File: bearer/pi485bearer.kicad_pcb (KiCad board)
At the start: 2 copper layers, 62 x 30 mm, 24 parts, among them P1 PWR, P2 Rasperry Pi, P5 CONN_01X04, P6 CONN_01X04, Q1 2N4401, Q2 2N4401, Q3 2N4401, U1 NE555

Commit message: Some additional cleanup and re-routing
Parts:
- removed MNT01 (x2), MNT02: MountingHole_2.2mm_M2, Mounting_Holes:MountingHole_2.2mm_M2
- removed RO: RO, Pin_Headers:Pin_Header_Straight_1x02
- removed TERM: TERM, Pin_Headers:Pin_Header_Straight_1x02
- added P3: RO, Pin_Headers:Pin_Header_Straight_1x02, F.Cu at (83.2, 24.8)
- added P4: TERM, Pin_Headers:Pin_Header_Straight_1x02, F.Cu at (94.6, 29.8)
- R7: value R -> 120
- moved R7 2.54 mm to (90.8, 33.0)
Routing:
- net GND: track 125.0 -> 128.6 mm
- net /lctec485/B: track 12.0 -> 10.8 mm
- net /lctec485/A: track 3.81 -> 4.86 mm
- net /lctec485/VCIN: track 90.0 -> 89.4 mm
- net Net-(P4-Pad2): track 4.34 -> 3.70 mm

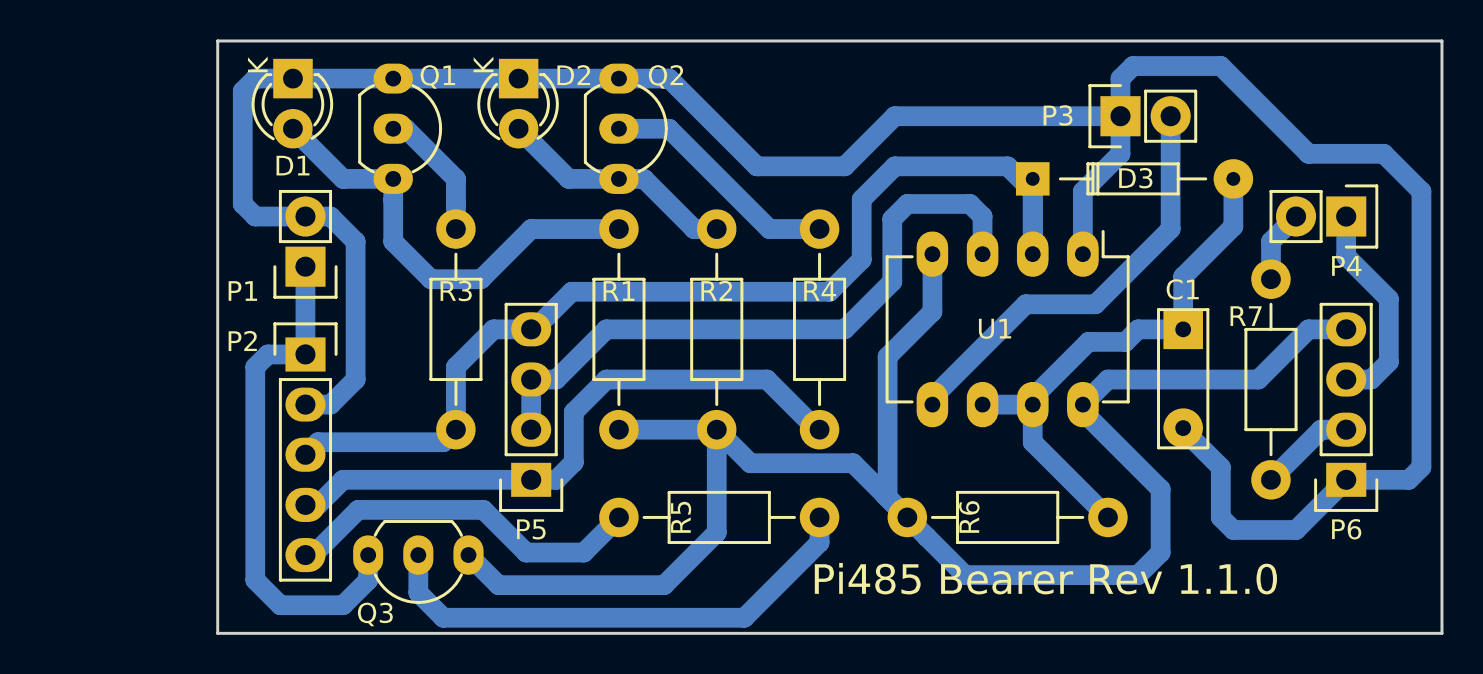
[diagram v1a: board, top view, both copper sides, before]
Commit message: Low-side NPN switching. We'll see if things 'floating' causes issues... if so, I'll have to order a few PNP's to use for high-side switching.
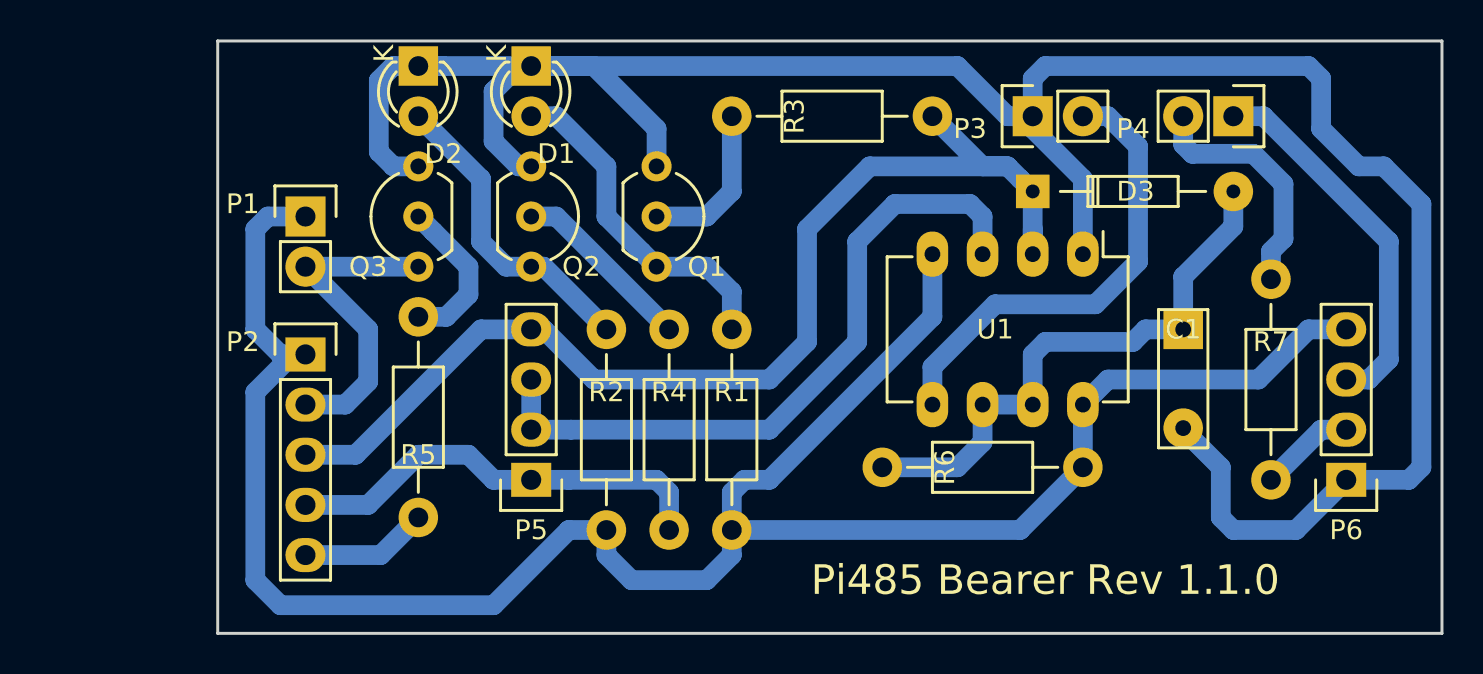
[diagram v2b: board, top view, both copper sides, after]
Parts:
- moved R5 22.7 mm to (47.6, 34.9), turned to 270 degrees
- moved R3 15.1 mm to (63.5, 24.8), turned to 0 degrees
- moved Q3 14.8 mm to (47.6, 32.4), turned to 90 degrees
- moved Q1 14.1 mm to (59.7, 27.3)
- moved D1 12.1 mm to (53.3, 22.2)
- moved R6 11.7 mm to (71.1, 42.5), turned to 0 degrees
- moved R4 9.16 mm to (60.3, 35.6)
- moved R1 7.65 mm to (63.5, 35.6)
- moved P4 7.65 mm to (88.9, 24.8)
- moved R2 7.55 mm to (57.1, 35.6)
- moved Q2 6.29 mm to (53.3, 27.3)
- moved D2 5.12 mm to (47.6, 22.2)
- moved P3 4.45 mm to (78.7, 24.8)
- moved P1 2.54 mm to (41.9, 29.8), turned to 0 degrees
- moved D3 0.63 mm to (78.7, 28.6)
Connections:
- C1 pad 2: GND -> /lctec485/GND
- D1 pad 1: GND -> /lctec485/GND
- D2 pad 1: GND -> /lctec485/GND
- P3 pad 1: GND -> /lctec485/GND
- P6 pad 1: GND -> /lctec485/GND
- P6 pad 4: /lctec485/VCIN -> VCC
- Q1 pad 1: Net-(D1-Pad2) -> /lctec485/GND
- Q1 pad 3: GND -> Net-(D1-Pad2)
- Q2 pad 1: Net-(D2-Pad2) -> /lctec485/GND
- Q2 pad 3: GND -> Net-(D2-Pad2)
- Q3 pad 1: VCC -> GND
- Q3 pad 3: /lctec485/VCIN -> /lctec485/GND
- R1 pad 2: /lctec485/VCIN -> VCC
- R2 pad 2: /lctec485/VCIN -> VCC
- R6 pad 2: /lctec485/VCIN -> VCC
- U1 pad 1: GND -> /lctec485/GND
- U1 pad 4: /lctec485/VCIN -> VCC
- U1 pad 8: /lctec485/VCIN -> VCC
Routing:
- net /lctec485/GND: track 0.00 -> 123.8 mm
- net GND: track 128.6 -> 16.5 mm
- net /lctec485/VCIN: track 89.4 -> 0.00 mm
- net VCC: track 26.1 -> 110.7 mm
- net Net-(Q3-Pad2): track 25.6 -> 8.01 mm
- net /(485PWR)_GPIO18: track 18.5 -> 7.06 mm
- net /(RXDO)_GPIO15: track 32.0 -> 22.3 mm
- net Net-(P4-Pad2): track 3.70 -> 12.4 mm
- net /lctec485/B: track 10.8 -> 19.1 mm
- net Net-(D1-Pad2): track 22.6 -> 17.2 mm
- net /(TXDO)_GPIO14: track 54.0 -> 58.3 mm
- net Net-(D2-Pad2): track 12.8 -> 15.9 mm
- net Net-(Q2-Pad2): track 12.3 -> 9.35 mm
- net /lctec485/DE: track 33.1 -> 35.3 mm
- net Net-(P3-Pad2): track 21.7 -> 23.8 mm
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
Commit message: high-side PNP power switching for the bearer.
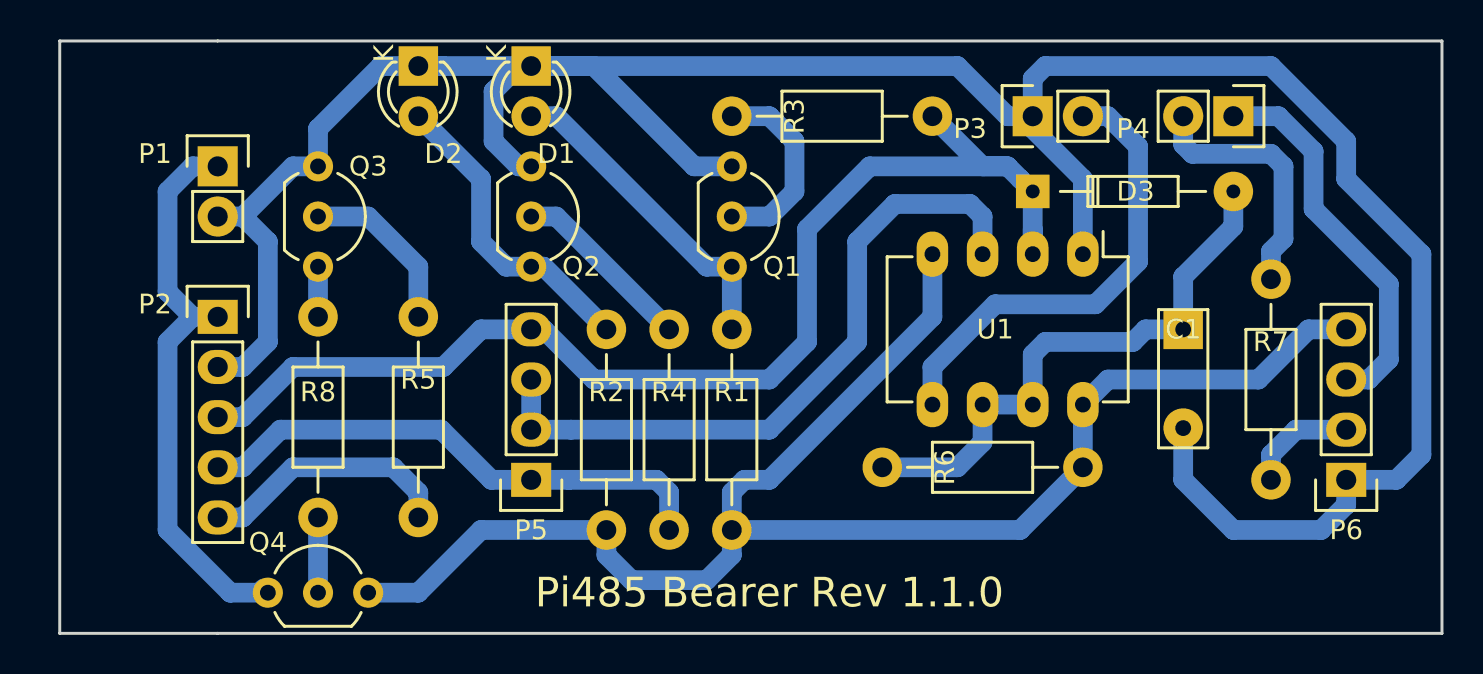
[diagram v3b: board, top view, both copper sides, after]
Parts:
- added Q4: 2N3906, TO_SOT_Packages_THT:TO-92_Inline_Wide, F.Cu at (40.0, 48.9)
- added R8: 270, Resistors_THT:Resistor_Horizontal_RM10mm, F.Cu at (42.5, 34.9)
- Q1, Q2, Q3: value 2N4401 -> 2N3904
- moved R5 10.2 mm to (47.6, 45.1), turned to 90 degrees
- moved Q3 7.18 mm to (42.5, 27.3), turned to 270 degrees
- moved P1 5.12 mm to (37.5, 27.3)
- moved P2 4.84 mm to (37.5, 34.9)
- moved Q1 3.81 mm to (63.5, 27.3)
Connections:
- C1 pad 2: /lctec485/GND -> GND
- D1 pad 1: /lctec485/GND -> GND
- D2 pad 1: /lctec485/GND -> GND
- P3 pad 1: /lctec485/GND -> GND
- P6 pad 1: /lctec485/GND -> GND
- P6 pad 4: VCC -> /lctec485/VCIN
- Q1 pad 1: /lctec485/GND -> GND
- Q2 pad 1: /lctec485/GND -> GND
- Q3 pad 3: /lctec485/GND -> Net-(Q3-Pad3)
- R1 pad 2: VCC -> /lctec485/VCIN
- R2 pad 2: VCC -> /lctec485/VCIN
- R5 pad 1: Net-(Q3-Pad2) -> /(485PWR)_GPIO18
- R5 pad 2: /(485PWR)_GPIO18 -> Net-(Q3-Pad2)
- R6 pad 2: VCC -> /lctec485/VCIN
- U1 pad 1: /lctec485/GND -> GND
- U1 pad 4: VCC -> /lctec485/VCIN
- U1 pad 8: VCC -> /lctec485/VCIN
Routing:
- net GND: track 16.5 -> 141.2 mm
- net /lctec485/GND: track 123.8 -> 0.00 mm
- net VCC: track 110.7 -> 28.8 mm
- net /lctec485/VCIN: track 0.00 -> 80.4 mm
- net /(485PWR)_GPIO18: track 7.06 -> 13.0 mm
- net /(RXDO)_GPIO15: track 22.3 -> 27.0 mm
- net /(TXDO)_GPIO14: track 58.3 -> 62.0 mm
- net Net-(Q4-Pad2): track 0.00 -> 3.24 mm
- net Net-(Q3-Pad3): track 0.00 -> 2.54 mm
- net Net-(Q1-Pad2): track 8.15 -> 9.94 mm
- net /lctec485/A: track 4.86 -> 5.61 mm
- net Net-(D1-Pad2): track 17.2 -> 16.5 mm
- net Net-(Q3-Pad2): track 8.01 -> 8.67 mm
- net Net-(P4-Pad2): track 12.4 -> 13.0 mm
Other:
- board size 62 x 30 mm -> 70 x 30 mm

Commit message: Esthetics and what-not...
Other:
- board text added: "+5v"
- board text added: "GND"
- board text added: "PWR"
- board text added: "RX"
- board text added: "TX"
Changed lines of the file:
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@@
     (links 44)
     (no_connects 0)
-    (area 37.389999 20.879999 99.540001 51.030001)
+    (area 29.389999 20.879999 99.540001 51.030001)
     (thickness 1.6)
-    (drawings 11)
+    (drawings 18)
     (tracks 176)
     (zones 0)
@@
     (36 B.SilkS user)
     (37 F.SilkS user)
-    (38 B.Mask user hide)
-    (39 F.Mask user hide)
+    (38 B.Mask user)
+    (39 F.Mask user)
     (40 Dwgs.User user)
     (41 Cmts.User user)
@@
     (descr "Resistor, Axial,  RM 10mm, 1/3W")
     (tags "Resistor Axial RM 10mm 1/3W")
-    (fp_text reference R8 (at 3.81 0 360) (layer F.SilkS)
+    (fp_text reference R8 (at 3.81 0) (layer F.SilkS)
       (effects (font (size 1 1) (thickness 0.15)))
     )
@@
     (descr "TO-92 leads in-line, wide, drill 0.8mm (see NXP sot054_po.pdf)")
     (tags "to-92 sc-43 sc-43a sot54 PA33 transistor")
-    (fp_text reference Q4 (at 0 -2.54 180) (layer F.SilkS)
+    (fp_text reference Q4 (at 5.715 -1.905 180) (layer F.SilkS)
       (effects (font (size 1 1) (thickness 0.15)))
     )
@@
     (descr "TO-92 leads in-line, wide, drill 0.8mm (see NXP sot054_po.pdf)")
     (tags "to-92 sc-43 sc-43a sot54 PA33 transistor")
-    (fp_text reference Q3 (at 0 -2.54 180) (layer F.SilkS)
+    (fp_text reference Q3 (at 5.08 -2.54 180) (layer F.SilkS)
       (effects (font (size 1 1) (thickness 0.15)))
     )
@@
       (effects (font (size 1 1) (thickness 0.15)))
     )
-    (fp_text value TERM (at -2.54 1.27) (layer F.Fab)
+    (fp_text value TERM (at -2.54 1.27 180) (layer F.SilkS)
       (effects (font (size 1 1) (thickness 0.15)))
     )
@@
       (effects (font (size 1 1) (thickness 0.15)))
     )
-    (fp_text value RO (at 2.54 1.27 180) (layer F.Fab)
+    (fp_text value RO (at 2.54 1.27 180) (layer F.SilkS)
       (effects (font (size 1 1) (thickness 0.15)))
     )
@@
     (descr "Through hole pin header")
     (tags "pin header")
-    (fp_text reference P1 (at -3.175 -0.635) (layer F.SilkS)
-      (effects (font (size 1 1) (thickness 0.15)))
-    )
-    (fp_text value PWR (at -3.175 1.905 90) (layer F.Fab)
+    (fp_text reference P1 (at 0 -2.54) (layer F.SilkS)
+      (effects (font (size 1 1) (thickness 0.15)))
+    )
+    (fp_text value PWR (at 2.54 0 -90) (layer F.Fab)
       (effects (font (size 1 1) (thickness 0.15)))
     )
@@
     (descr "Through hole pin header")
     (tags "pin header")
-    (fp_text reference P2 (at -3.175 -0.635) (layer F.SilkS)
-      (effects (font (size 1 1) (thickness 0.15)))
-    )
-    (fp_text value "Rasperry Pi" (at -3.175 6.35 90) (layer F.Fab)
+    (fp_text reference P2 (at 0 -2.54 180) (layer F.SilkS)
+      (effects (font (size 1 1) (thickness 0.15)))
+    )
+    (fp_text value "Rasperry Pi" (at 2.54 2.54 -90) (layer F.Fab)
       (effects (font (size 1 1) (thickness 0.15)))
     )
@@
     )
   )
+  (gr_text GND (at 36.195 29.845) (layer F.SilkS)
+    (effects (font (size 1.5 1.5) (thickness 0.2)) (justify right))
+  )
+  (gr_text +5v (at 35.915 27.305) (layer F.SilkS)
+    (effects (font (size 1.5 1.5) (thickness 0.2)) (justify right))
+  )
+  (gr_text PWR (at 36.195 45.085) (layer F.SilkS)
+    (effects (font (size 1.5 1.5) (thickness 0.2)) (justify right))
+  )
+  (gr_text RX (at 36.195 42.545) (layer F.SilkS)
+    (effects (font (size 1.5 1.5) (thickness 0.2)) (justify right))
+  )
+  (gr_text TX (at 36.195 40.005) (layer F.SilkS)
+    (effects (font (size 1.5 1.5) (thickness 0.2)) (justify right))
+  )
+  (gr_text GND (at 36.195 37.465) (layer F.SilkS)
+    (effects (font (size 1.5 1.5) (thickness 0.2)) (justify right))
+  )
+  (gr_text +5v (at 35.915 34.925) (layer F.SilkS)
+    (effects (font (size 1.5 1.5) (thickness 0.2)) (justify right))
+  )
   (target plus (at 32.480254 48.055446) (size 5) (width 0.15) (layer Edge.Cuts))
   (gr_line (start 29.465 50.955) (end 37.465 50.955) (layer Edge.Cuts) (width 0.15))
@@
   (target plus (at 96.465 47.955) (size 5) (width 0.15) (layer Edge.Cuts))
   (target plus (at 96.465 23.955) (size 5) (width 0.15) (layer Edge.Cuts))
-  (gr_text "Pi485 Bearer Rev 1.1.0" (at 65.405 48.895) (layer F.SilkS)
-    (effects (font (size 1.5 1.5) (thickness 0.3)))
+  (gr_text "Pi485 Bearer Rev 1.1.0" (at 66.675 48.895) (layer F.SilkS)
+    (effects (font (size 2 2) (thickness 0.4)))
   )
   (gr_line (start 99.465 20.955) (end 99.465 50.955) (layer Edge.Cuts) (width 0.15))

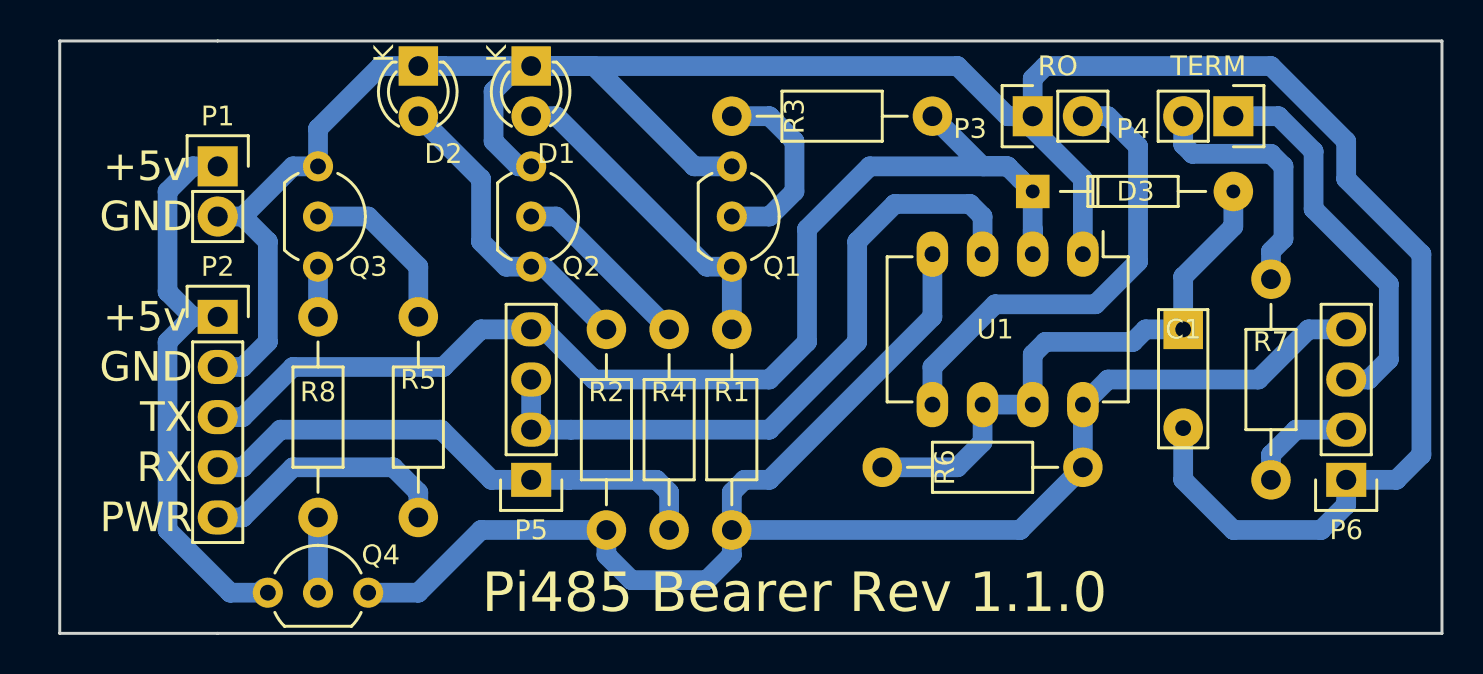
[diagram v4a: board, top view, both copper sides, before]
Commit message: Moved the P1 P2 connectors to make a bit more sense, enlarged the bearer to 70mm, four mount holes per board.
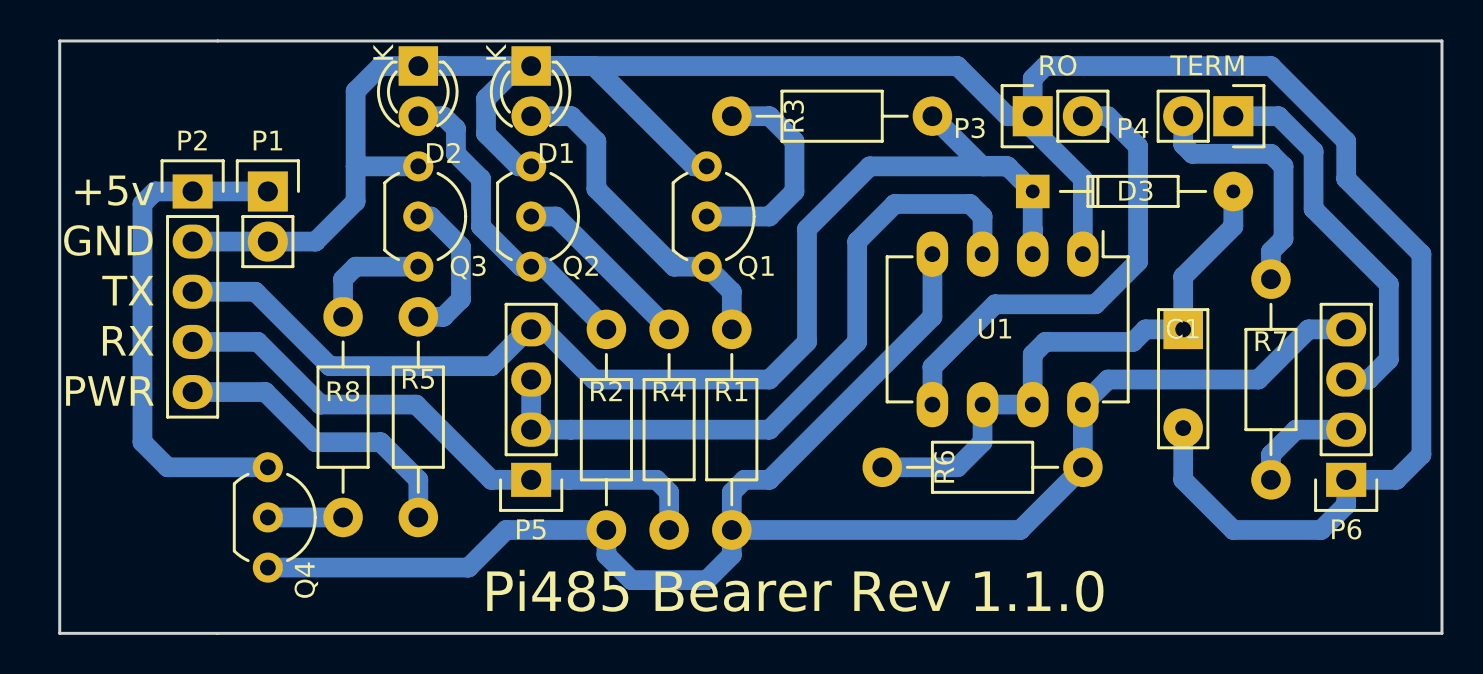
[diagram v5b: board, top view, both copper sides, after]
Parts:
- moved P2 6.48 mm to (36.2, 28.6)
- moved Q4 6.35 mm to (40.0, 42.5), turned to 270 degrees
- moved Q3 5.08 mm to (47.6, 27.3)
- moved P1 2.84 mm to (40.0, 28.6)
- moved Q1 1.27 mm to (62.2, 27.3)
- moved R8 1.27 mm to (43.8, 34.9)
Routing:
- net /lctec485/VCIN: track 80.4 -> 85.0 mm
- net GND: track 141.2 -> 137.4 mm
- net Net-(Q3-Pad3): track 2.54 -> 5.98 mm
- net VCC: track 28.8 -> 25.6 mm
- net /(RXDO)_GPIO15: track 27.0 -> 29.3 mm
- net /(485PWR)_GPIO18: track 13.0 -> 15.2 mm
- net /(TXDO)_GPIO14: track 62.0 -> 63.6 mm
- net Net-(Q1-Pad2): track 9.94 -> 11.2 mm
- net Net-(Q3-Pad2): track 8.67 -> 7.98 mm
- net Net-(D1-Pad2): track 16.5 -> 17.2 mm
- net Net-(Q4-Pad2): track 3.24 -> 3.81 mm
